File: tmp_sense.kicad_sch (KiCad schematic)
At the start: 0 parts

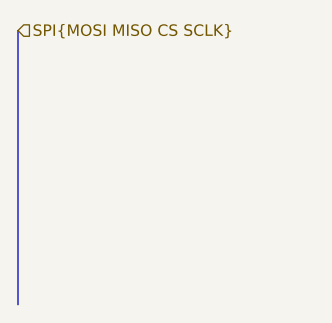
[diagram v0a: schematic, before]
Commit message: Add Teensy 4.1, current sensing, a 5 V input and MD jumpers
The netlist goes from 66 parts and 28 nets to 105 parts and 79 nets.

Schematic edits by Luke
- U2, a Teensy 4.1 on socket strips, replaces the MCU headers. Pins 2 to 6
  go to VG0 to VG4 through 0 ohm links R22 to R26. Pin 7 goes to the Q6 gate
  through jumper J9. Pins 10 to 13 carry the SPI labels. A1 and A2 read the
  two current-sense outputs.
- U3 and U4, INA190A5 amplifiers across shunts R4 and R3, through 0 ohm
  links R29 to R32. Each output has a 1k and 100n filter (R27 with C12,
  R28 with C15).
- J8 is now a +5V banana jack to the Teensy VIN, with C16 to C19 and
  Schottky D2 from +5V to GND.
- A +3V3 rail from the Teensy 3V3 pin, with C5, C13, C14, C20, C21 and C22.
- MD control uses three 2-pin jumpers, J9, J10 and J11. R15 and R16 are
  removed. R18 is the 10k pull-up behind J11.
- R19 and R20, 0 ohm across the two shunts, both marked DNP. R21, 0 ohm
  between VOUT and the load resistors.
- C6 changed from 1u 0805 to 10u 1206.
- Test points TP20 to TP29.
- Global labels SHUNT_IN_A, SHUNT_IN_B, SHUNT_OUT_A and SHUNT_OUT_B on the
  shunt nodes.

Field edits by Claude
- Footprint and part fields on the twelve 0 ohm resistors (R19 to R26, R29
  to R32), Vishay CRCW08050000Z0EAHP.
- Part fields on TP14 to TP19 and TP22 to TP29, Keystone 5005.
- Description on J9, J10 and J11.
A netlist export before and after those edits has identical nets and values.

ERC reports 0 errors and 40 warnings.

Co-Authored-By: Claude Opus 5.5 (1M context) <noreply@anthropic.com>
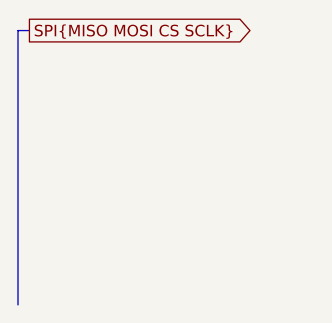
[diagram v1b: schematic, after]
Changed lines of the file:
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@@
+	(bus
+		(pts
+			(xy 198.12 46.99) (xy 199.39 46.99)
+		)
+		(stroke
+			(width 0)
+			(type default)
+		)
+	)
 	(bus
 		(pts
@@
 		)
 	)
-	(hierarchical_label "SPI{MOSI MISO CS SCLK}"
-		(shape input)
-		(at 198.12 46.99 0)
+	(global_label "SPI{MISO MOSI CS SCLK}"
+		(shape output)
+		(at 199.39 46.99 0)
+		(fields_autoplaced yes)
 		(effects
 			(font
@@
 			(justify left)
 		)
+		(property "Intersheetrefs" "${INTERSHEET_REFS}"
+			(at 226.5052 46.99 0)
+			(hide yes)
+			(show_name no)
+			(do_not_autoplace no)
+			(effects
+				(font
+					(size 1.27 1.27)
+				)
+				(justify left)
+			)
+		)
 	)
